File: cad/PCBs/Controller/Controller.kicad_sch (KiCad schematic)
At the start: 10 parts, among them U1 74HC595, U2 74HC595, U3 BH1750FVI-TR, U4 HDC2080

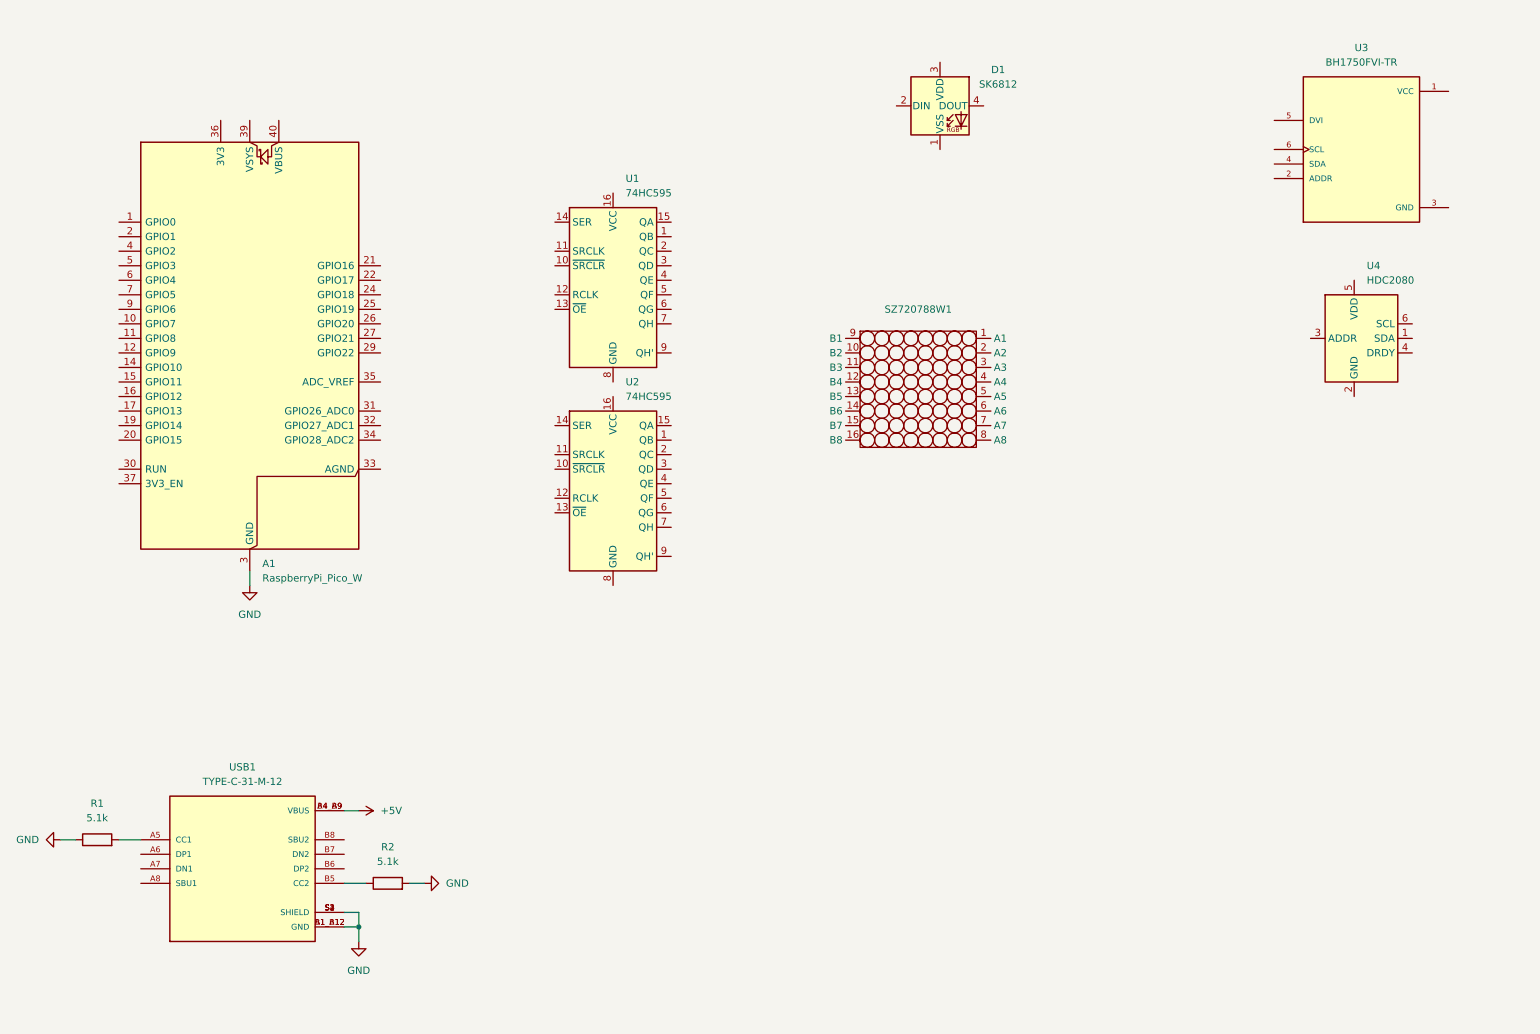
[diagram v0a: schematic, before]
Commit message: Initial Digit Component Placement
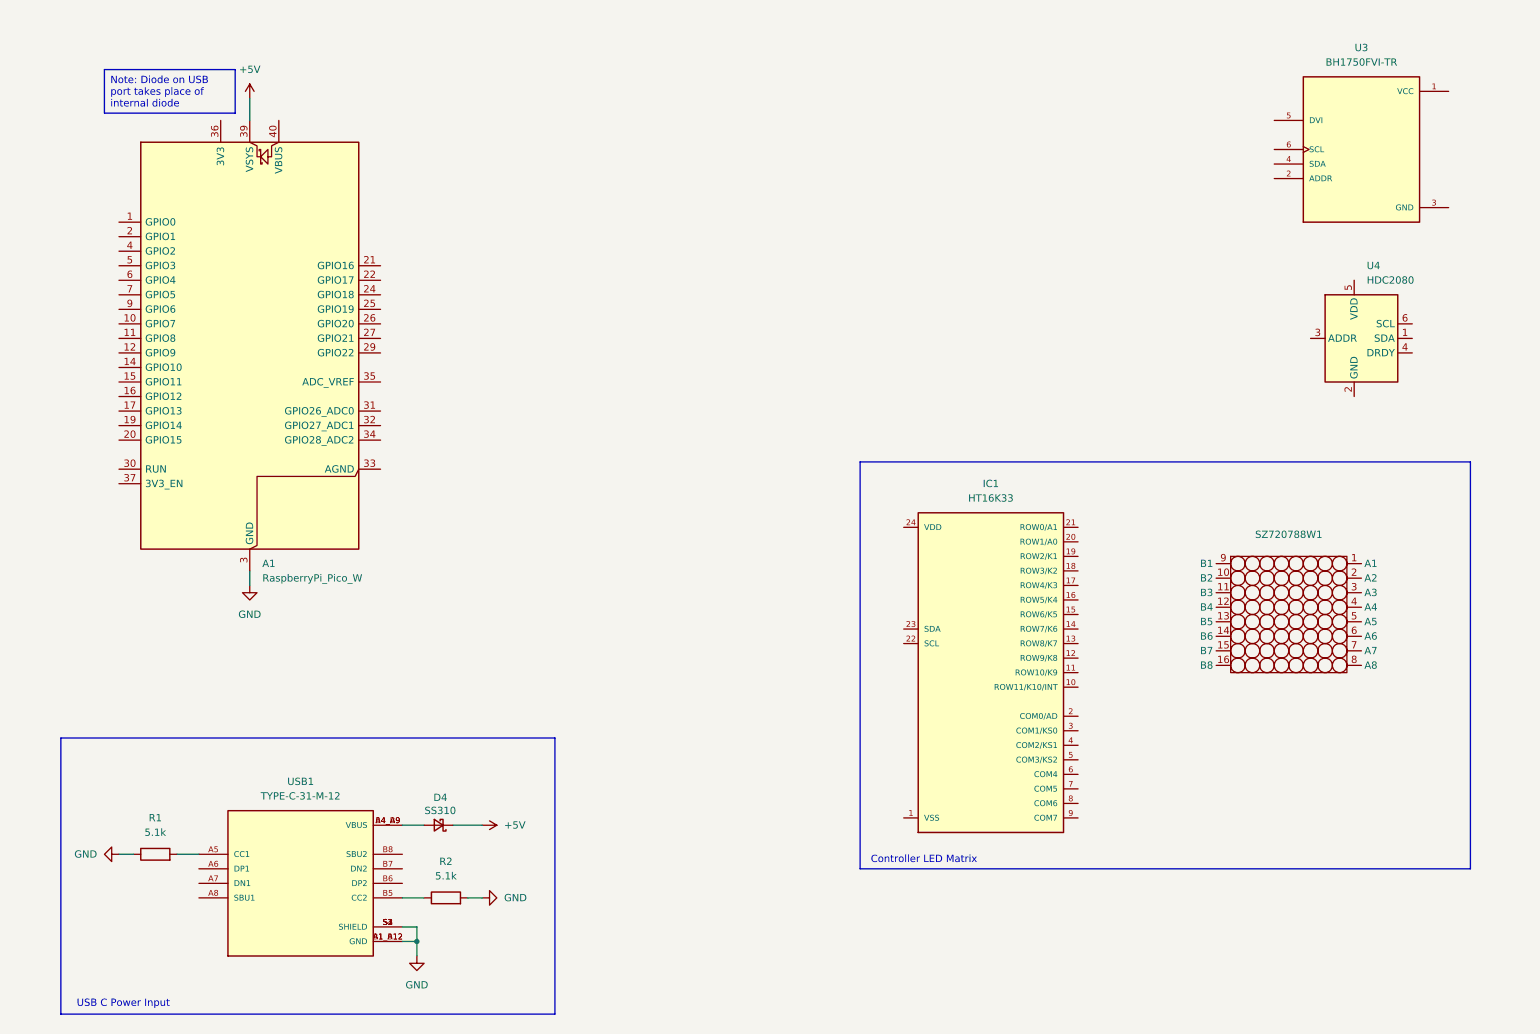
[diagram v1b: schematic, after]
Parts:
- removed D1: SK6812, LED_SMD:LED_SK6812_PLCC4_5.0x5.0mm_P3.2mm, symbol LED:SK6812
- removed U1, U2: 74HC595, Package_DIP:DIP-16_W7.62mm_Socket, symbol 74xx:74HC595
- added D4: SS310, Diode_SMD:D_SOD-323F, symbol Device:D_Schottky_Small
- added IC1: HT16K33, HT16K33:HT16K33, symbol HT16K33:HT16K33
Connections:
- net +5V: now also A1.39 (VSYS), D4.1 (K); no longer USB1.A4_B9 (VBUS), USB1.B4_A9 (VBUS)
- new net: D4.2 (A), USB1.A4_B9 (VBUS), USB1.B4_A9 (VBUS)
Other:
- note added: "Controller LED Matrix"
- note added: "USB C Power Input"
- moved on the sheet: R1, R2, SZ720788W1, USB1

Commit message: Connected Controller Components, updated matrix footprint
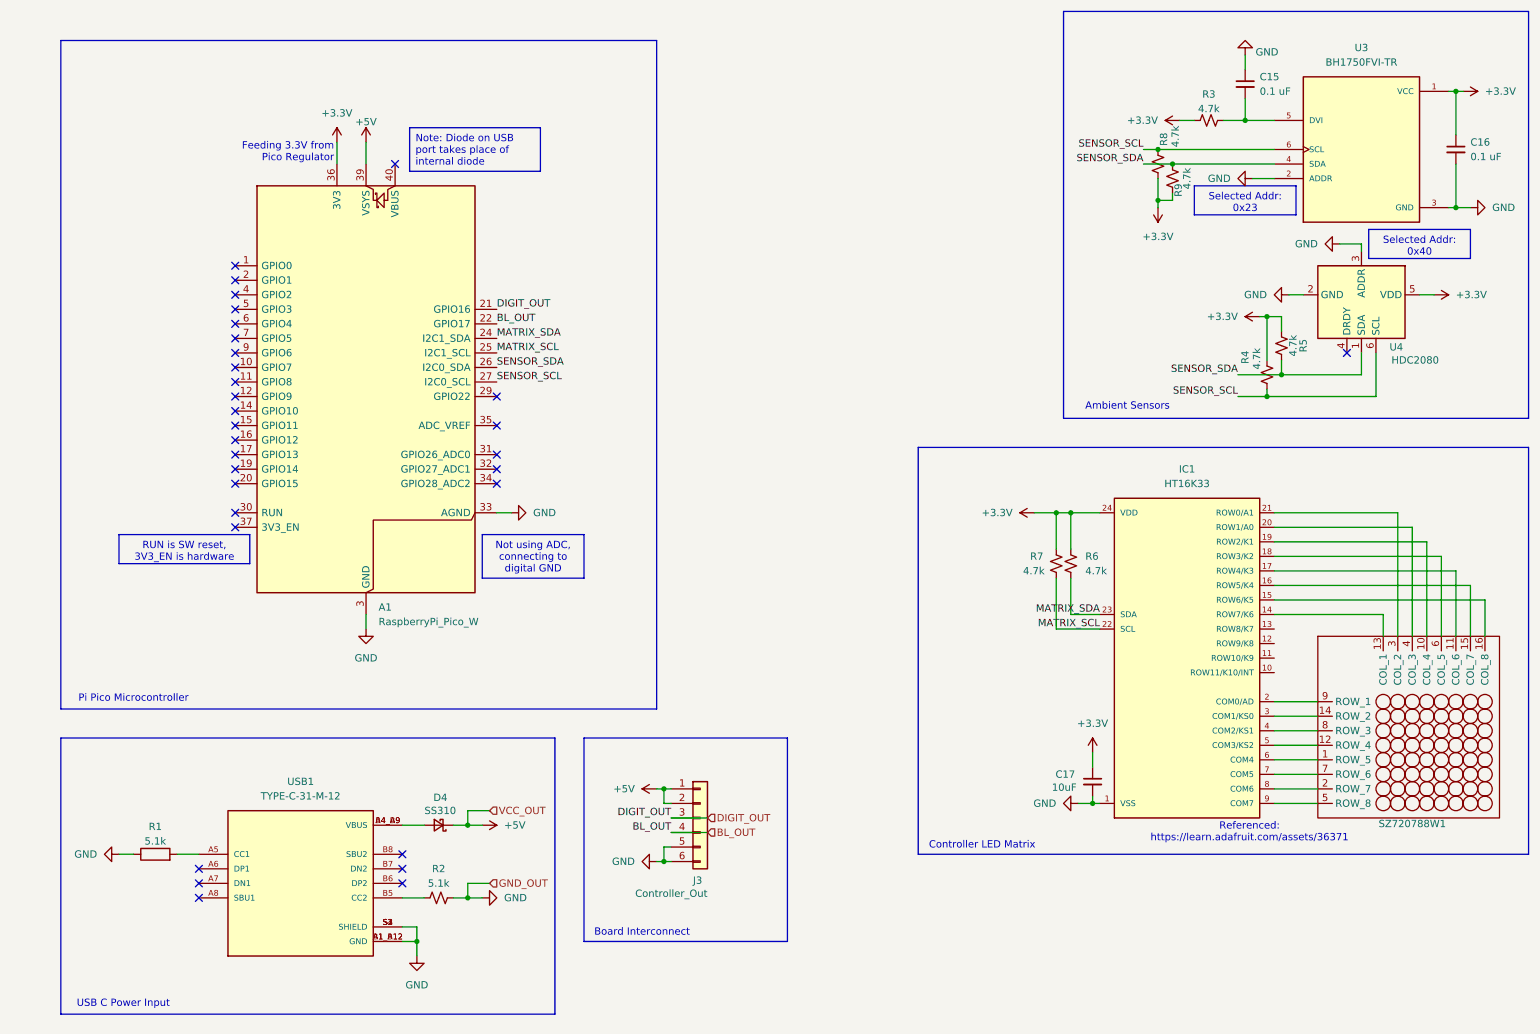
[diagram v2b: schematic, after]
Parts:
- added C15, C16: 0.1 uF, Capacitor_SMD:C_0805_2012Metric, symbol Device:C_Small
- added C17: 10uF, Capacitor_SMD:C_0805_2012Metric, symbol Device:C_Small
- added J3: Controller_Out, Connector_PinHeader_2.54mm:PinHeader_1x06_P2.54mm_Horizontal, symbol Connector_Generic:Conn_01x06
- added R3, R4, R5, R6, R7, R8, R9: 4.7k, Resistor_SMD:R_0805_2012Metric, symbol Device:R_Small_US
- R2: symbol Device:R -> Device:R_Small_US
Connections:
- net +5V: now also J3.1 (Pin_1), J3.2 (Pin_2)
- net GND: now also A1.33 (AGND), IC1.1 (VSS), U3.2 (ADDR), U3.3 (GND), U4.2 (GND), U4.3 (ADDR), C15.1, C16.2, C17.2, J3.5 (Pin_5), J3.6 (Pin_6)
- net at SZ720788W1.1 (ROW_5): now also IC1.6 (COM4)
- net at SZ720788W1.10 (COL_4): now also IC1.19 (ROW2/K1)
- net at SZ720788W1.11 (COL_6): now also IC1.17 (ROW4/K3)
- net at SZ720788W1.12 (ROW_4): now also IC1.5 (COM3/KS2)
- net at SZ720788W1.13 (COL_1): now also IC1.14 (ROW7/K6)
- net at SZ720788W1.14 (ROW_2): now also IC1.3 (COM1/KS0)
- net at SZ720788W1.15 (COL_7): now also IC1.16 (ROW5/K4)
- net at SZ720788W1.16 (COL_8): now also IC1.15 (ROW6/K5)
- net at SZ720788W1.2 (ROW_7): now also IC1.8 (COM6)
- net at SZ720788W1.3 (COL_2): now also IC1.21 (ROW0/A1)
- net at SZ720788W1.4 (COL_3): now also IC1.20 (ROW1/A0)
- net at SZ720788W1.5 (ROW_8): now also IC1.9 (COM7)
- net at SZ720788W1.6 (COL_5): now also IC1.18 (ROW3/K2)
- net at SZ720788W1.7 (ROW_6): now also IC1.7 (COM5)
- net at SZ720788W1.8 (ROW_3): now also IC1.4 (COM2/KS1)
- net at SZ720788W1.9 (ROW_1): now also IC1.2 (COM0/AD)
- net SENSOR_SDA: now reaches U4.1 (SDA)
- net SENSOR_SDA: now also A1.26 (GPIO20), U3.4 (SDA), R5.2, R9.1
- net +3.3V: now reaches U4.5 (VDD)
- net +3.3V: now also A1.36 (3V3), IC1.24 (VDD), U3.1 (VCC), C16.1, C17.1, R3.1, R4.2, R5.1, R6.1, R7.1, R8.1, R9.2
- net SENSOR_SCL: now reaches U4.6 (SCL)
- net SENSOR_SCL: now also A1.27 (GPIO21), U3.6 (SCL), R4.1, R8.2
- net at U3.5 (DVI): now also C15.2, R3.2
- net MATRIX_SCL: now reaches IC1.22 (SCL)
- net MATRIX_SCL: now also A1.25 (GPIO19), R7.2
- net MATRIX_SDA: now reaches IC1.23 (SDA)
- net MATRIX_SDA: now also A1.24 (GPIO18), R6.2
- net DIGIT_OUT: now reaches A1.21 (GPIO16)
- net DIGIT_OUT: now also J3.3 (Pin_3)
- net BL_OUT: now reaches A1.22 (GPIO17)
- net BL_OUT: now also J3.4 (Pin_4)
- no-connect marks 0 -> 31
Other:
- note added: "Ambient Sensors"
- note added: "Board Interconnect"
- note added: "Feeding 3.3V from Pico Regulator"
- note added: "Pi Pico Microcontroller"
- note added: "Referenced: https://learn.adafruit.com/assets/36371"
- moved on the sheet: A1, IC1, SZ720788W1, U4

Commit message: WIP Routing Controller
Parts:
- removed R1: 5.1k, Resistor_SMD:R_2010_5025Metric, symbol Device:R
- added R1: 5.1k, Resistor_SMD:R_0805_2012Metric, symbol Device:R_Small_US
- R2: footprint Resistor_SMD:R_2010_5025Metric -> Resistor_SMD:R_0805_2012Metric
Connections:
- net GND: now also R1.1
- net at USB1.A5 (CC1): now also R1.2
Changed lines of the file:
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@@
 	(wire
 		(pts
-			(xy 33.02 162.56) (xy 35.56 162.56)
+			(xy 35.56 162.56) (xy 38.1 162.56)
 		)
 		(stroke
@@
 	(label "MATRIX_SDA"
 		(at 204.47 120.65 180)
+		(fields_autoplaced yes)
 		(effects
 			(font
@@
 	(label "MATRIX_SCL"
 		(at 204.47 123.19 180)
+		(fields_autoplaced yes)
 		(effects
 			(font
@@
 	(label "MATRIX_SDA"
 		(at 99.06 72.39 0)
+		(fields_autoplaced yes)
 		(effects
 			(font
@@
 	(label "MATRIX_SCL"
 		(at 99.06 74.93 0)
+		(fields_autoplaced yes)
 		(effects
 			(font
@@
 	)
 	(symbol
-		(lib_id "Device:R")
-		(at 39.37 162.56 90)
-		(unit 1)
-		(exclude_from_sim no)
-		(in_bom yes)
-		(on_board yes)
-		(dnp no)
-		(property "Reference" "R1"
-			(at 39.37 157.734 90)
-			(effects
-				(font
-					(size 1.27 1.27)
-				)
-			)
-		)
-		(property "Value" "5.1k"
-			(at 39.37 160.274 90)
-			(effects
-				(font
-					(size 1.27 1.27)
-				)
-			)
-		)
-		(property "Footprint" "Resistor_SMD:R_2010_5025Metric"
-			(at 39.37 164.338 90)
-			(effects
-				(font
-					(size 1.27 1.27)
-				)
-				(hide yes)
-			)
-		)
-		(property "Datasheet" "~"
-			(at 39.37 162.56 0)
-			(effects
-				(font
-					(size 1.27 1.27)
-				)
-				(hide yes)
-			)
-		)
-		(property "Description" "Resistor"
-			(at 39.37 162.56 0)
-			(effects
-				(font
-					(size 1.27 1.27)
-				)
-				(hide yes)
-			)
-		)
-		(pin "1"
-		)
-		(pin "2"
-		)
-		(instances
-			(project "RGB_Segment_Clock"
-				(path "/40bfd19c-28ae-4125-bffd-c1ba01268b82/ddbd17b6-28a0-495f-a062-2182329bea65"
-					(reference "R1")
-					(unit 1)
-				)
-			)
-		)
-	)
-	(symbol
 		(lib_id "Device:R_Small_US")
 		(at 214.63 41.91 180)
@@
 			)
 		)
-		(property "Footprint" "Resistor_SMD:R_2010_5025Metric"
+		(property "Footprint" "Resistor_SMD:R_0805_2012Metric"
 			(at 88.9 170.18 0)
 			(effects
@@
 	(symbol
 		(lib_id "power:GND")
-		(at 33.02 162.56 270)
+		(at 35.56 162.56 270)
 		(unit 1)
 		(exclude_from_sim no)
@@
 		(fields_autoplaced yes)
 		(property "Reference" "#PWR01"
-			(at 26.67 162.56 0)
+			(at 29.21 162.56 0)
 			(effects
 				(font
@@
 		)
 		(property "Value" "GND"
-			(at 29.21 162.5599 90)
+			(at 31.75 162.5599 90)
 			(effects
 				(font
@@
 		)
 		(property "Footprint" ""
-			(at 33.02 162.56 0)
+			(at 35.56 162.56 0)
 			(effects
 				(font
@@
 		)
 		(property "Datasheet" ""
-			(at 33.02 162.56 0)
+			(at 35.56 162.56 0)
 			(effects
 				(font
@@
 		)
 		(property "Description" "Power symbol creates a global label with name \"GND\" , ground"
-			(at 33.02 162.56 0)
+			(at 35.56 162.56 0)
 			(effects
 				(font
@@
 					(unit 1)
 				)
+			)
+		)
+	)
+	(symbol
+		(lib_id "Device:R_Small_US")
+		(at 40.64 162.56 90)
+		(unit 1)
+		(exclude_from_sim no)
+		(in_bom yes)
+		(on_board yes)
+		(dnp no)
+		(property "Reference" "R1"
+			(at 40.64 157.48 90)
+			(effects
+				(font
+					(size 1.27 1.27)
+				)
+			)
+		)
+		(property "Value" "5.1k"
+			(at 40.64 160.02 90)
+			(effects
+				(font
+					(size 1.27 1.27)
+				)
+			)
+		)
+		(property "Footprint" "Resistor_SMD:R_0805_2012Metric"
+			(at 40.64 162.56 0)
+			(effects
+				(font
+					(size 1.27 1.27)
+				)
+				(hide yes)
+			)
+		)
+		(property "Datasheet" "~"
+			(at 40.64 162.56 0)
+			(effects
+				(font
+					(size 1.27 1.27)
+				)
+				(hide yes)
+			)
+		)
+		(property "Description" "Resistor, small US symbol"
+			(at 40.64 162.56 0)
+			(effects
+				(font
+					(size 1.27 1.27)
+				)
+				(hide yes)
+			)
+		)
+		(pin "1"
+		)
+		(pin "2"
+		)
+		(instances
+			(project "RGB_Segment_Clock"
+				(path "/40bfd19c-28ae-4125-bffd-c1ba01268b82/ddbd17b6-28a0-495f-a062-2182329bea65"
+					(reference "R1")
+					(unit 1)
+				)

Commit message: WIP Integrating USB C PD
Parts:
- removed D4: SS310, Diode_SMD:D_SOD-323F, symbol Device:D_Schottky_Small
- removed R1, R2: 5.1k, Resistor_SMD:R_0805_2012Metric, symbol Device:R_Small_US
- removed USB1: TYPE-C-31-M-12, TYPE-C-31-M-12:HRO_TYPE-C-31-M-12, symbol TYPE-C-31-M-12:TYPE-C-31-M-12
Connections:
- net +5V: no longer J3.2 (Pin_2)
- no-connect marks 31 -> 25
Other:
- added sheet USB_Power (USB_Power.kicad_sch)
- note removed: "USB C Power Input"
- moved on the sheet: A1, J3
